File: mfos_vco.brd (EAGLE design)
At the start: 100 x 80 mm, 64 parts, among them IC1 TL072P, IC2 LM394N, IC3 TL072P, IC4 TL072P, U1 2N5457, X3 22-23-2051

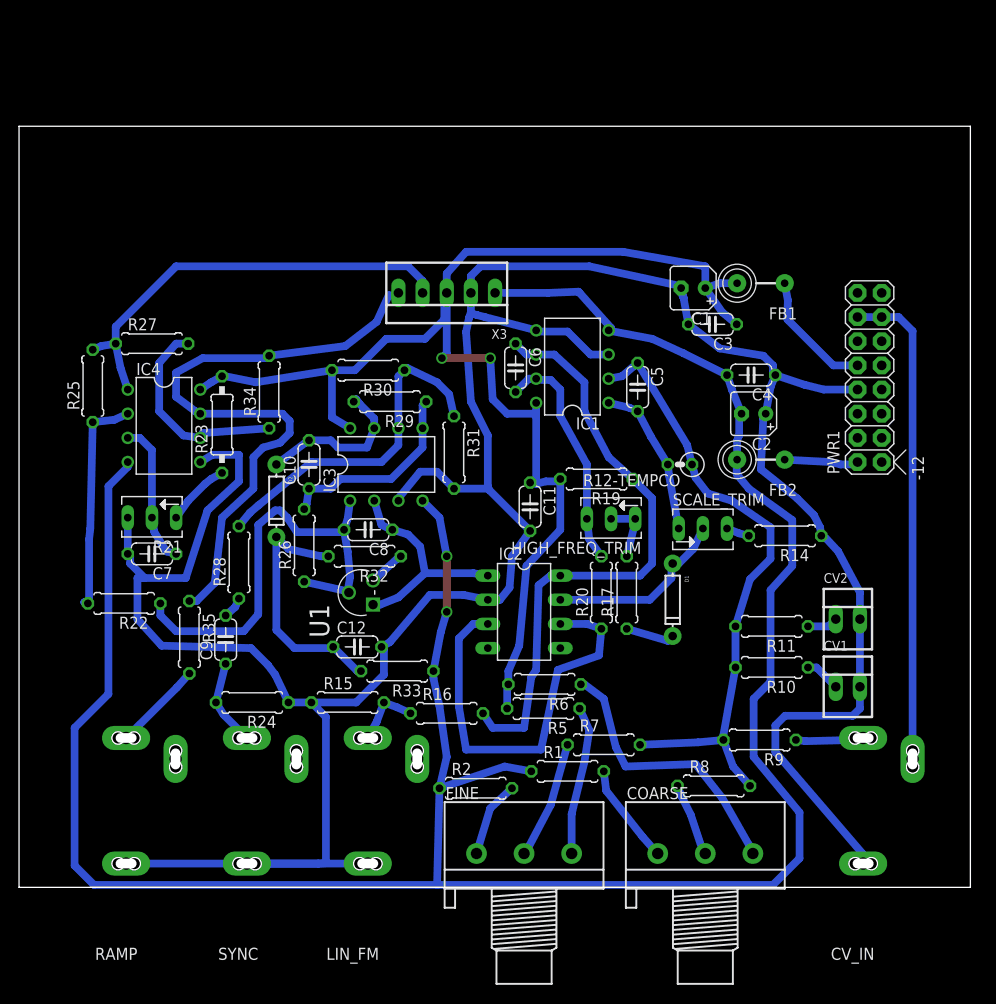
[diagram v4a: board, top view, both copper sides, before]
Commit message: thicker traces
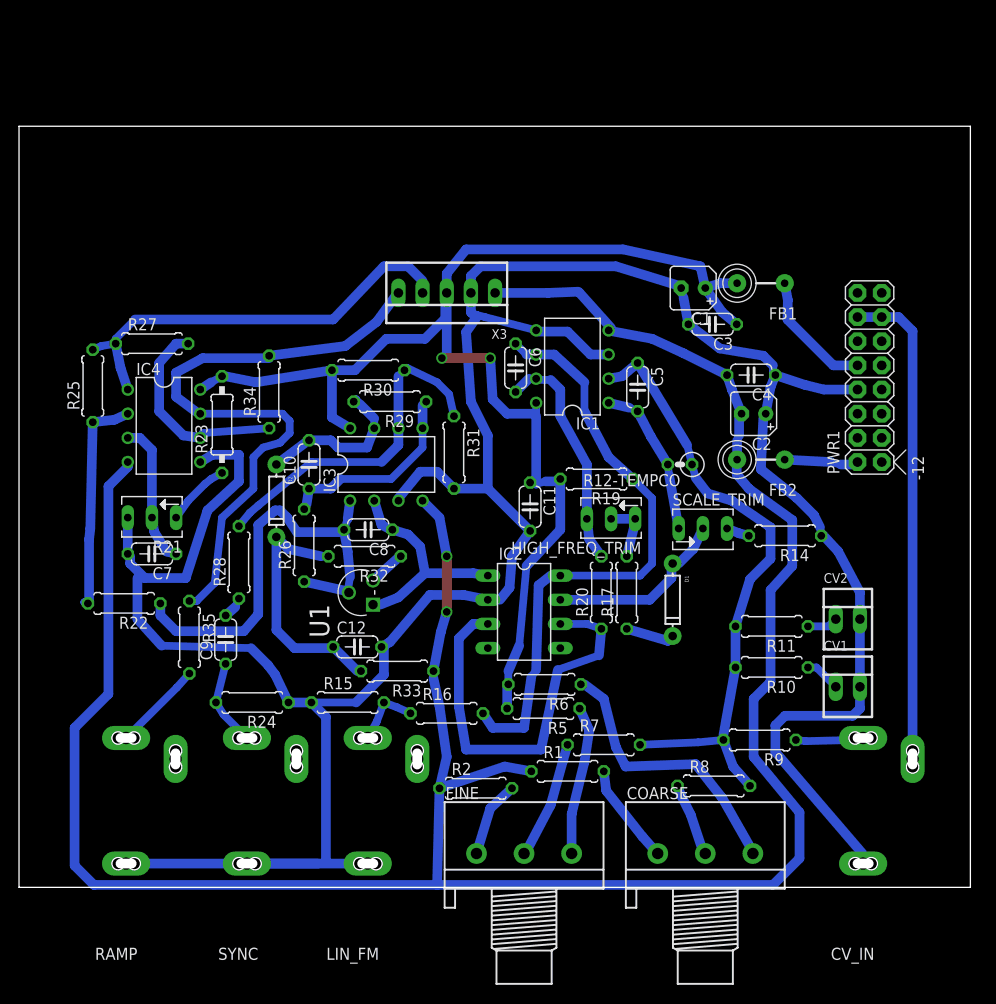
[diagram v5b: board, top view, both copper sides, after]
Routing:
- net N$33: track 46.1 -> 45.4 mm
- net GND: track 317.8 -> 318.4 mm

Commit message: cutout and thicker traces
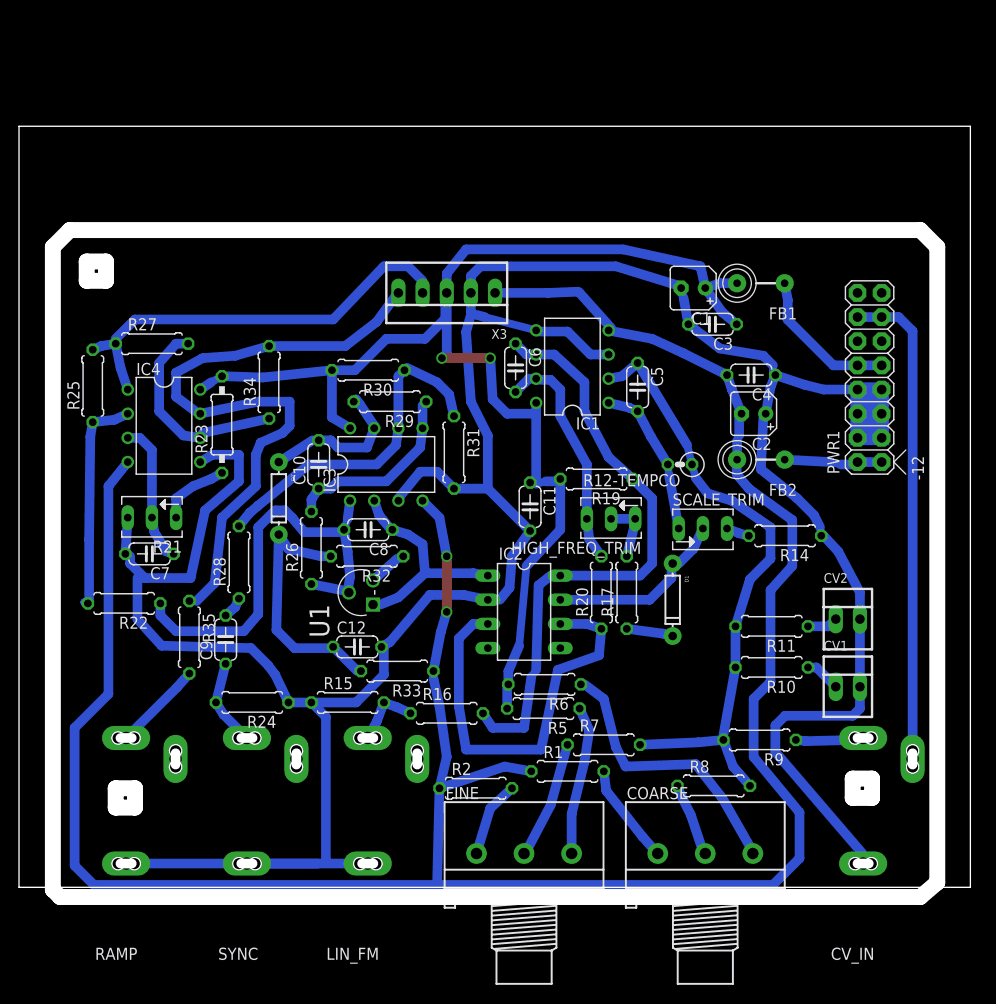
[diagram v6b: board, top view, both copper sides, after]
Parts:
- moved C10 1.02 mm to (31.5, 44.5)
- moved R34 1.02 mm to (26.3, 53.1)
- moved R26 0.80 mm to (30.7, 35.7)
- moved D2 0.36 mm to (27.3, 40.9)
- moved C7 0.25 mm to (13.7, 35.1)
- moved R32 0.25 mm to (36.6, 34.8)
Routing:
- net N$39: track 7.80 -> 10.3 mm
- net N$38: track 13.2 -> 15.7 mm
- net N$35: track 66.0 -> 67.5 mm
- net N$21: track 47.8 -> 46.8 mm
- net N$22: track 20.9 -> 20.1 mm
- net N$27: track 6.82 -> 7.58 mm
- net N$30: track 17.0 -> 16.4 mm
- net N$32: track 26.6 -> 27.2 mm
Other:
- board size 100 x 80 mm -> 100 x 81 mm

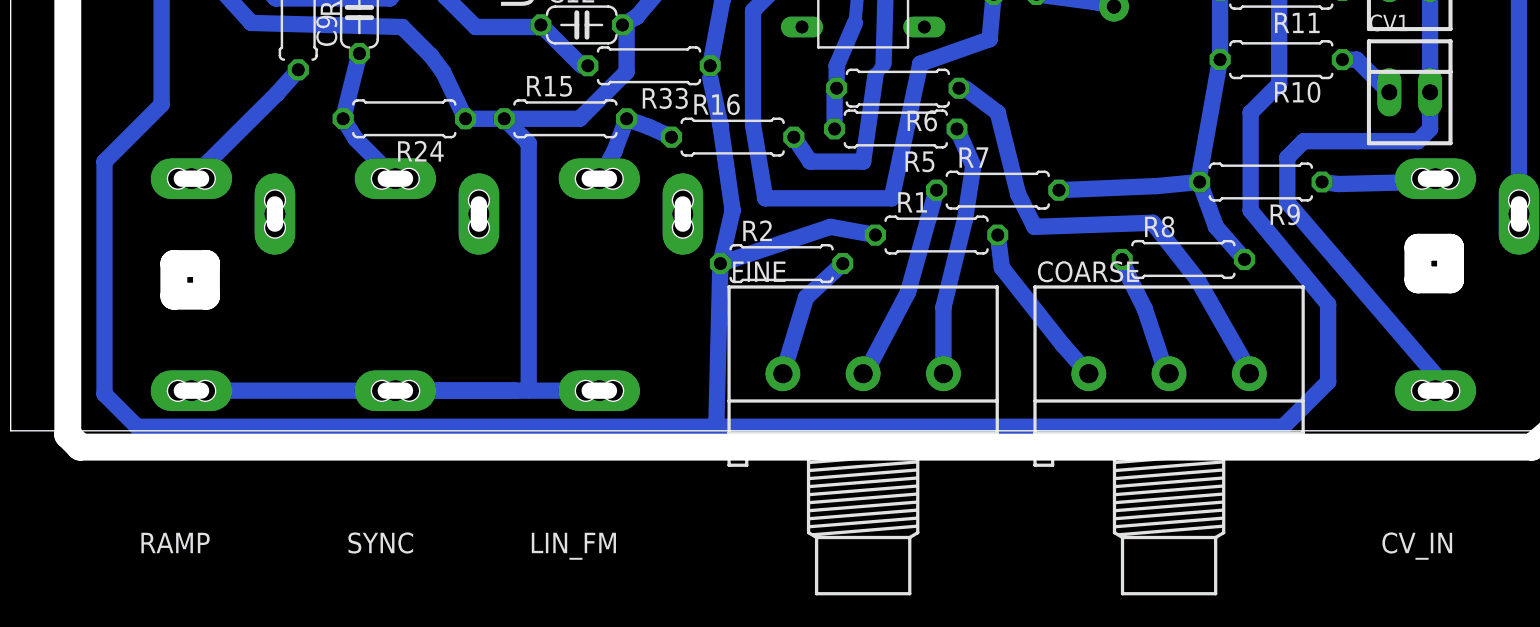
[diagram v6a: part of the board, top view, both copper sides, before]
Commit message: moved negative trace away from front panel edge
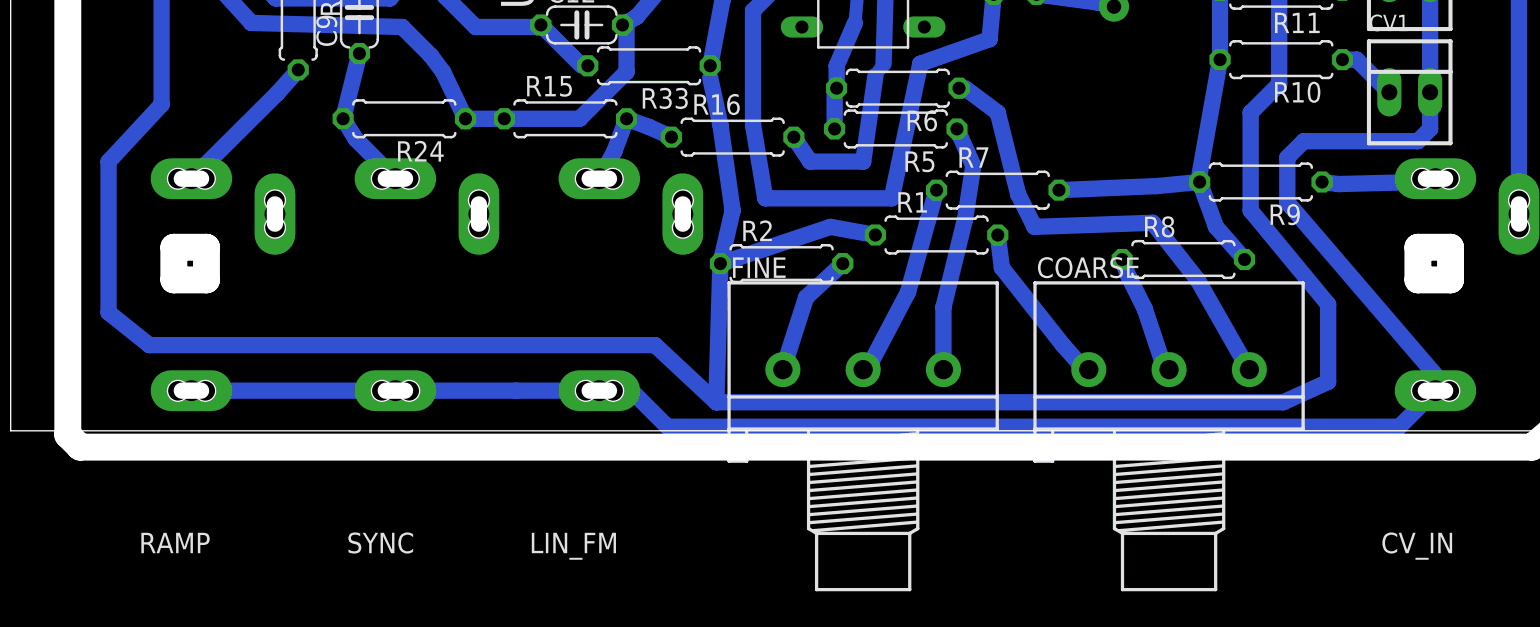
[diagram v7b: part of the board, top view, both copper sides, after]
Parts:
- moved COARSE 0.25 mm to (72.1, 3.81)
- moved FINE 0.25 mm to (53.1, 3.81)
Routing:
- net GND: track 318.6 -> 347.5 mm
- net -12V: track 260.0 -> 253.4 mm
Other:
- outline, holes or cut-outs redrawn
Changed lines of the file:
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@@
 <wire x1="89.662" y1="9.398" x2="87.63" y2="9.398" width="1.6764" layer="46"/>
 <wire x1="87.63" y1="9.398" x2="87.63" y2="11.43" width="1.6764" layer="46"/>
-<wire x1="10.16" y1="10.414" x2="12.192" y2="10.414" width="1.6764" layer="46"/>
-<wire x1="12.192" y1="10.414" x2="12.192" y2="8.382" width="1.6764" layer="46"/>
-<wire x1="12.192" y1="8.382" x2="10.16" y2="8.382" width="1.6764" layer="46"/>
-<wire x1="10.16" y1="8.382" x2="10.16" y2="10.414" width="1.6764" layer="46"/>
+<wire x1="10.16" y1="11.43" x2="12.192" y2="11.43" width="1.6764" layer="46"/>
+<wire x1="12.192" y1="11.43" x2="12.192" y2="9.398" width="1.6764" layer="46"/>
+<wire x1="12.192" y1="9.398" x2="10.16" y2="9.398" width="1.6764" layer="46"/>
+<wire x1="10.16" y1="9.398" x2="10.16" y2="11.43" width="1.6764" layer="46"/>
 <rectangle x1="87.376" y1="46.482" x2="91.44" y2="53.086" layer="16"/>
 </plain>
@@
 <element name="C12" library="rcl" package="C050-024X044" value="100pF" x="35.56" y="25.273"/>
 <element name="C10" library="rcl" package="C050-024X044" value="4p7F" x="31.496" y="44.45" rot="R90"/>
-<element name="COARSE" library="pot" package="3RP/1610N" value="100k" x="72.136" y="3.556"/>
+<element name="COARSE" library="pot" package="3RP/1610N" value="100k" x="72.136" y="3.81"/>
 <element name="CV_IN" library="erthenvar" package="ERTHENVAR-JACK-90DEG" value="AUDIO-JACK" x="93.726" y="0" rot="R180"/>
 <element name="D1" library="SparkFun-DiscreteSemi" package="DIODE-1N4148" value="" x="68.707" y="30.226" rot="R270"/>
 <element name="D2" library="SparkFun-DiscreteSemi" package="DIODE-1N4148" value="" x="27.305" y="40.894" rot="R270"/>
-<element name="FINE" library="pot" package="3RP/1610N" value="100k" x="53.086" y="3.556"/>
+<element name="FINE" library="pot" package="3RP/1610N" value="100k" x="53.086" y="3.81"/>
 <element name="IC1" library="linear" package="DIL08" value="TL072P" x="58.166" y="54.737" rot="R90"/>
 <element name="IC3" library="linear" package="DIL08" value="TL072P" x="38.608" y="44.45"/>
@@
 <wire x1="61.722" y1="10.16" x2="65.532" y2="5.334" width="1.016" layer="16"/>
 <wire x1="65.532" y1="5.334" x2="66.882" y2="3.81" width="1.016" layer="16"/>
-<wire x1="66.882" y1="3.81" x2="67.136" y2="3.556" width="0.8128" layer="16"/>
+<wire x1="66.882" y1="3.81" x2="67.136" y2="3.81" width="0.8128" layer="16"/>
 </signal>
 <signal name="N$2">
@@
 <contactref element="FINE" pad="1"/>
 <wire x1="51.816" y1="10.414" x2="49.53" y2="8.302" width="1.016" layer="16"/>
-<wire x1="49.53" y1="8.302" x2="48.086" y2="3.556" width="1.016" layer="16"/>
+<wire x1="49.53" y1="8.302" x2="48.086" y2="3.81" width="1.016" layer="16"/>
 </signal>
 <signal name="N$3">
 <contactref element="R5" pad="1"/>
 <contactref element="FINE" pad="3"/>
-<wire x1="58.086" y1="3.556" x2="58.086" y2="7.7" width="1.016" layer="16"/>
+<wire x1="58.086" y1="3.81" x2="58.086" y2="7.7" width="1.016" layer="16"/>
 <wire x1="58.086" y1="7.7" x2="59.436" y2="13.208" width="1.016" layer="16"/>
 <wire x1="59.436" y1="13.208" x2="59.944" y2="16.51" width="1.016" layer="16"/>
@@
 <wire x1="71.12" y1="12.954" x2="73.914" y2="9.398" width="1.016" layer="16"/>
 <wire x1="73.914" y1="9.398" x2="76.708" y2="4.492" width="1.016" layer="16"/>
-<wire x1="76.708" y1="4.492" x2="77.136" y2="3.556" width="0.8128" layer="16"/>
+<wire x1="76.708" y1="4.492" x2="77.136" y2="3.81" width="0.8128" layer="16"/>
 <wire x1="59.055" y1="21.336" x2="59.436" y2="21.336" width="0.8128" layer="16"/>
 <wire x1="59.436" y1="21.336" x2="61.468" y2="19.812" width="1.016" layer="16"/>
@@
 <wire x1="11.43" y1="44.704" x2="9.398" y2="42.164" width="1.016" layer="16"/>
 <wire x1="9.398" y1="42.164" x2="9.398" y2="20.32" width="1.016" layer="16"/>
-<wire x1="9.398" y1="20.32" x2="5.842" y2="16.764" width="1.016" layer="16"/>
-<wire x1="5.842" y1="16.764" x2="5.842" y2="2.286" width="1.016" layer="16"/>
-<wire x1="5.842" y1="2.286" x2="7.874" y2="0.254" width="1.016" layer="16"/>
-<wire x1="7.874" y1="0.254" x2="43.942" y2="0.254" width="1.016" layer="16"/>
-<wire x1="44.196" y1="10.414" x2="43.942" y2="0.254" width="1.016" layer="16"/>
+<wire x1="9.398" y1="20.32" x2="6.096" y2="16.764" width="1.016" layer="16"/>
+<wire x1="6.096" y1="16.764" x2="6.096" y2="7.366" width="1.016" layer="16"/>
+<wire x1="6.096" y1="7.366" x2="8.636" y2="5.334" width="1.016" layer="16"/>
+<wire x1="8.636" y1="5.334" x2="40.132" y2="5.334" width="1.016" layer="16"/>
+<wire x1="40.132" y1="5.334" x2="43.942" y2="1.778" width="1.016" layer="16"/>
+<wire x1="44.196" y1="10.414" x2="43.942" y2="1.778" width="1.016" layer="16"/>
 <wire x1="75.478" y1="44.958" x2="75.478" y2="46.95" width="1.016" layer="16"/>
 <wire x1="75.478" y1="46.95" x2="75.692" y2="47.498" width="0.8128" layer="16"/>
@@
 <wire x1="75.946" y1="49.784" x2="74.93" y2="52.324" width="1.016" layer="16"/>
 <wire x1="74.93" y1="52.324" x2="74.422" y2="53.848" width="1.016" layer="16"/>
-<wire x1="43.942" y1="0.254" x2="79.248" y2="0.254" width="1.016" layer="16"/>
-<wire x1="79.248" y1="0.254" x2="82.042" y2="3.048" width="1.016" layer="16"/>
+<wire x1="43.942" y1="1.778" x2="79.248" y2="1.778" width="1.016" layer="16"/>
+<wire x1="79.248" y1="1.778" x2="82.042" y2="3.048" width="1.016" layer="16"/>
 <wire x1="82.042" y1="3.048" x2="82.042" y2="7.874" width="1.016" layer="16"/>
 <wire x1="82.042" y1="7.874" x2="77.216" y2="13.716" width="1.016" layer="16"/>
@@
 <contactref element="R7" pad="1"/>
 <contactref element="FINE" pad="2"/>
-<wire x1="53.086" y1="3.556" x2="53.34" y2="3.81" width="0.8128" layer="16"/>
+<wire x1="53.086" y1="3.81" x2="53.34" y2="3.81" width="0.8128" layer="16"/>
 <wire x1="53.34" y1="3.81" x2="55.88" y2="8.636" width="1.016" layer="16"/>
 <wire x1="55.88" y1="8.636" x2="57.15" y2="13.208" width="1.016" layer="16"/>
@@
 <wire x1="69.596" y1="9.652" x2="70.612" y2="7.62" width="1.016" layer="16"/>
 <wire x1="70.612" y1="7.62" x2="71.882" y2="3.81" width="1.016" layer="16"/>
-<wire x1="71.882" y1="3.81" x2="72.136" y2="3.556" width="0.8128" layer="16"/>
+<wire x1="71.882" y1="3.81" x2="72.136" y2="3.81" width="0.8128" layer="16"/>
 </signal>
 <signal name="N$7">
@@
 <wire x1="28.321" y1="19.177" x2="28.321" y2="19.431" width="0.8128" layer="16"/>
 <wire x1="11.256" y1="2.5" x2="23.956" y2="2.5" width="1.016" layer="16"/>
-<wire x1="23.956" y1="2.5" x2="36.656" y2="2.5" width="1.016" layer="16"/>
+<wire x1="31.456" y1="2.5" x2="36.656" y2="2.5" width="1.016" layer="16"/>
 <wire x1="36.656" y1="2.5" x2="36.87" y2="2.5" width="0.8128" layer="16"/>
 <wire x1="36.87" y1="2.5" x2="37.084" y2="2.286" width="0.8128" layer="16"/>
@@
 <wire x1="23.956" y1="2.5" x2="31.456" y2="2.5" width="1.016" layer="16"/>
 <wire x1="31.456" y1="2.5" x2="32.258" y2="2.54" width="0.8128" layer="16"/>
-<wire x1="32.258" y1="2.54" x2="32.258" y2="17.907" width="1.016" layer="16"/>
-<wire x1="32.258" y1="17.907" x2="30.734" y2="19.431" width="1.016" layer="16"/>
 <wire x1="30.734" y1="19.431" x2="35.433" y2="19.431" width="1.016" layer="16"/>
 <wire x1="35.433" y1="19.431" x2="38.354" y2="22.352" width="1.016" layer="16"/>
@@
 <wire x1="57.658" y1="58.42" x2="54.483" y2="58.42" width="1.016" layer="16"/>
 <wire x1="54.483" y1="58.42" x2="54.356" y2="58.547" width="0.8128" layer="16"/>
+<wire x1="36.656" y1="2.5" x2="38.648" y2="2.5" width="1.016" layer="16"/>
+<wire x1="38.648" y1="2.5" x2="40.894" y2="0.254" width="1.016" layer="16"/>
+<wire x1="40.894" y1="0.254" x2="86.48" y2="0.254" width="1.016" layer="16"/>
+<wire x1="86.48" y1="0.254" x2="88.726" y2="2.5" width="1.016" layer="16"/>
 <wire x1="90.678" y1="49.784" x2="90.678" y2="52.324" width="0" layer="19" extent="1-1"/>
 <wire x1="88.138" y1="49.784" x2="90.678" y2="49.784" width="0" layer="19" extent="1-1"/>
